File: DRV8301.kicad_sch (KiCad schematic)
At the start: 38 parts, among them U2 LM3671, U3 DRV8301

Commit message: started power stage
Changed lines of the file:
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@@
 	(text "C2923951"
 		(exclude_from_sim no)
-		(at 207.01 39.37 0)
+		(at 195.834 43.434 0)
 		(effects
 			(font

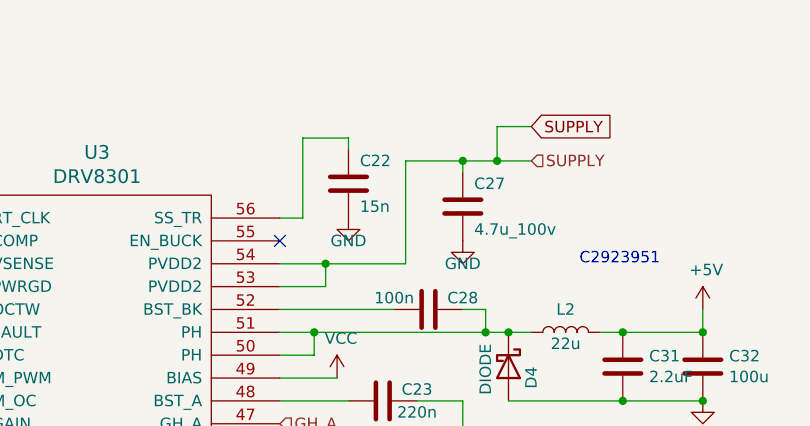
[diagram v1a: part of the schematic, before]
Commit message: changed connectors, needs final routing and drc
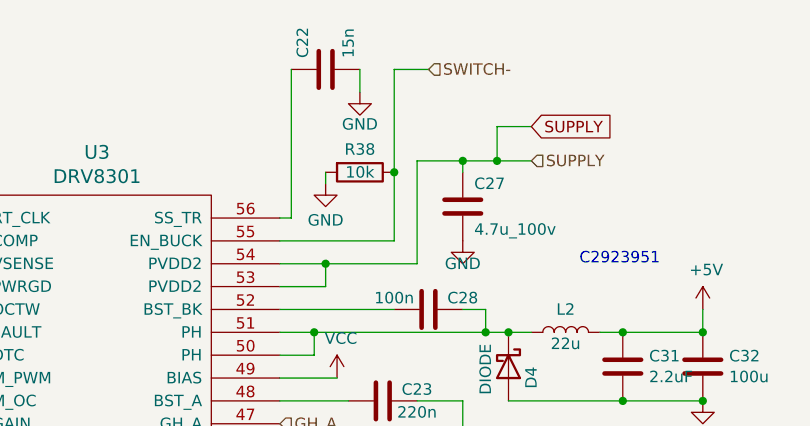
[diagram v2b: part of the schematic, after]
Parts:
- added R38: 10k, Resistor_SMD:R_0603_1608Metric, symbol Device:R
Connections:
- net GND: now also R38.2
- net SWITCH-: now reaches U3.55 (EN_BUCK)
- net SWITCH-: now also R38.1
- no-connect marks 6 -> 5
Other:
- moved on the sheet: C22

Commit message: Finished routing
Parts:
- C26, C27: LCSC part no. C385986 -> C385987
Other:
- note removed: "C2923951"
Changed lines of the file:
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@@
 		(comment 1 "Drawn By: CG")
 	)
-	(text "C2923951"
-		(exclude_from_sim no)
-		(at 195.834 43.434 0)
-		(effects
-			(font
-				(size 1.27 1.27)
-			)
-			(justify left bottom)
-		)
-	)
 	(junction
 		(at 200.66 58.42)
@@
 			)
 		)
-		(property "LCSC part no." "C385986"
+		(property "LCSC part no." "C385987"
 			(at 182.88 36.83 0)
 			(effects
@@
 			)
 		)
-		(property "LCSC part no." "C385986"
+		(property "LCSC part no." "C385987"
 			(at 168.91 114.3 0)
 			(effects

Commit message: Release1
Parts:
- C26, C27: Link https://jlcpcb.com/partdetail/TaiyoYuden-HMK325C7475KMHPE/C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 -> (none); MFP HMK325C7475KMHPE -> (none)
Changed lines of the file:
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@@
 			)
 		)
-		(property "Datasheet" "https://datasheet.lcsc.com/lcsc/2211282230_Taiyo-Yuden-HMK325C7475KMHPE_C385986.pdf"
+		(property "Datasheet" ""
 			(at 182.88 36.83 0)
 			(effects
@@
 			)
 		)
-		(property "Link" "https://jlcpcb.com/partdetail/TaiyoYuden-HMK325C7475KMHPE/C385986"
+		(property "Link" ""
 			(at 182.88 36.83 0)
 			(effects
@@
 			)
 		)
-		(property "MFP" "HMK325C7475KMHPE"
+		(property "MFP" ""
 			(at 182.88 36.83 0)
 			(effects
@@
 			)
 		)
-		(property "Datasheet" "https://datasheet.lcsc.com/lcsc/2211282230_Taiyo-Yuden-HMK325C7475KMHPE_C385986.pdf"
+		(property "Datasheet" ""
 			(at 168.91 114.3 0)
 			(effects
@@
 			)
 		)
-		(property "Link" "https://jlcpcb.com/partdetail/TaiyoYuden-HMK325C7475KMHPE/C385986"
+		(property "Link" ""
 			(at 168.91 114.3 0)
 			(effects
@@
 			)
 		)
-		(property "MFP" "HMK325C7475KMHPE"
+		(property "MFP" ""
 			(at 168.91 114.3 0)
 			(effects
